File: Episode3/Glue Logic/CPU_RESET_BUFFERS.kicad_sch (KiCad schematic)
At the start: 28 parts, among them SW1 RST SW, U1 74AHCT541, U2 74HC245, U3 HD63C09P, U4 74AHCT541, U5 74AHCT244, U6 MIC1232

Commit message: Pushing back everything, due to PC reinstall.
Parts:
- removed RN6: 130Ω, Package_DIP:DIP-16_W7.62mm, symbol Device:R_Pack08
- removed U5: 74AHCT244, Package_DIP:DIP-20_W7.62mm_Socket, symbol 74xx:74HC244
- added R3, R4, R5: 100Ω, symbol Device:R_Small_US
- added U6: 74HCT125, symbol 74xx:74LS125
- U2: renamed from U6; symbol 6309 v2.0:MIC1232 -> MicroHobbyist:MIC1232
- U3: renamed from U1; value 74AHCT541 -> 74HCT541
- U4: value 74AHCT541 -> 74HCT541
- U5: renamed from U2; value 74HC245 -> 74HCT245
- renumbered R4 to R2, RN3 to RN1, RN4 to RN2, RN1 to RN3, RN5 to RN4, RN2 to RN5, U3 to U1
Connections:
- net UB_BS is gone; now on net BS: U1.5 (BS)
- net UB_Q is gone; now on net Q: U1.35 (Q)
- net +5V: now also U6.14 (VCC)
- net BA: now also R5.2; no longer U3.1 (G1), U4.1 (G1), U5.19 (CE)
- net E: now also R4.2
- net GND: now also U6.10, U6.12, U6.13, U6.4, U6.7 (GND)
- net R/~{W}: now also R3.2
- net UB_BA: now also U3.1 (G1), U4.1 (G1), U5.19 (CE), U6.1, U6.9
- net UB_E: now also U6.5
- net UB_R/~{W}: now also U6.2
- net ~{BREQ}: now also RN2.2 (R1); no longer RN2.4 (R3)
- net ~{HALT}: now also RN2.3 (R2); no longer RN2.2 (R1)
- net ~{MRDY}: now also RN2.4 (R3); no longer RN2.3 (R2)
- net ~{RST_{trigger}}: no longer names the net of SW1.2, U2.1 (~{PBRST})
- new net: R3.1, U6.3
- new net: R5.1, U6.8
- new net: R4.1, U6.6
- no-connect marks 4 -> 2
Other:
- moved on the sheet: JP1, R2, RN1, RN2, RN3, RN4, RN5, SW1, U1, U2

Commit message: Major updates to PLDs
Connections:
- net Q: now also U2.7 (~{ST})
- net UB_E: no longer U2.7 (~{ST})
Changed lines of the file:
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@@
+	)
+	(junction
+		(at 105.41 99.06)
+		(diameter 0)
+		(color 0 0 0 0)
 	)
 	(junction
@@
 	)
 	(junction
-		(at 105.41 96.52)
-		(diameter 0)
-		(color 0 0 0 0)
-	)
-	(junction
 		(at 44.45 68.58)
 		(diameter 0)
@@
 	(wire
 		(pts
-			(xy 105.41 96.52) (xy 179.07 96.52)
+			(xy 95.25 96.52) (xy 179.07 96.52)
 		)
 		(stroke
@@
 	(wire
 		(pts
+			(xy 105.41 99.06) (xy 240.03 99.06)
+		)
+		(stroke
+			(width 0)
+			(type default)
+		)
+	)
+	(wire
+		(pts
 			(xy 62.23 55.88) (xy 69.85 55.88)
 		)
@@
 		)
 	)
-	(wire
-		(pts
-			(xy 95.25 96.52) (xy 105.41 96.52)
-		)
-		(stroke
-			(width 0)
-			(type default)
-		)
-	)
 	(bus
 		(pts
@@
 	(wire
 		(pts
-			(xy 95.25 99.06) (xy 240.03 99.06)
+			(xy 95.25 99.06) (xy 105.41 99.06)
 		)
 		(stroke
@@
 	(wire
 		(pts
+			(xy 105.41 99.06) (xy 105.41 123.19)
+		)
+		(stroke
+			(width 0)
+			(type default)
+		)
+	)
+	(wire
+		(pts
 			(xy 224.79 45.72) (xy 232.41 45.72)
 		)
@@
 		)
 		(stroke
-			(width 0)
-			(type default)
-		)
-	)
-	(wire
-		(pts
-			(xy 105.41 96.52) (xy 105.41 123.19)
-		)
-		(stroke

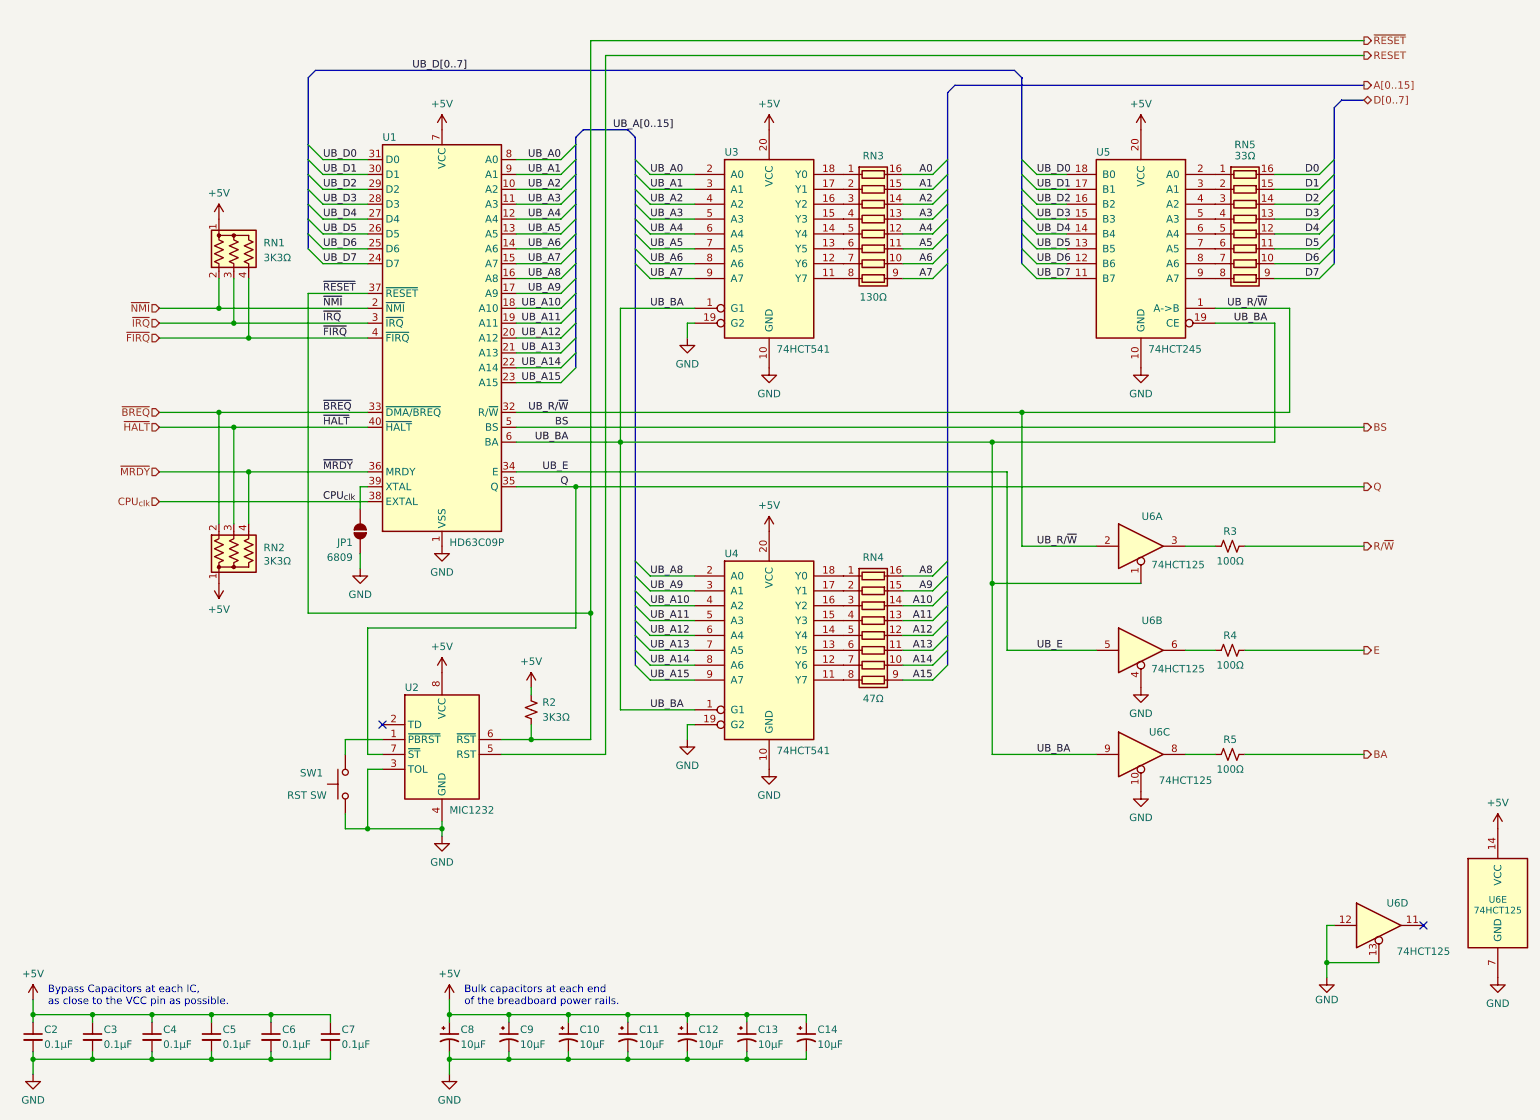
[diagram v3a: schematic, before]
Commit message: Reduced PLDs from 5 to 4, and optimized macrocells to the maximum
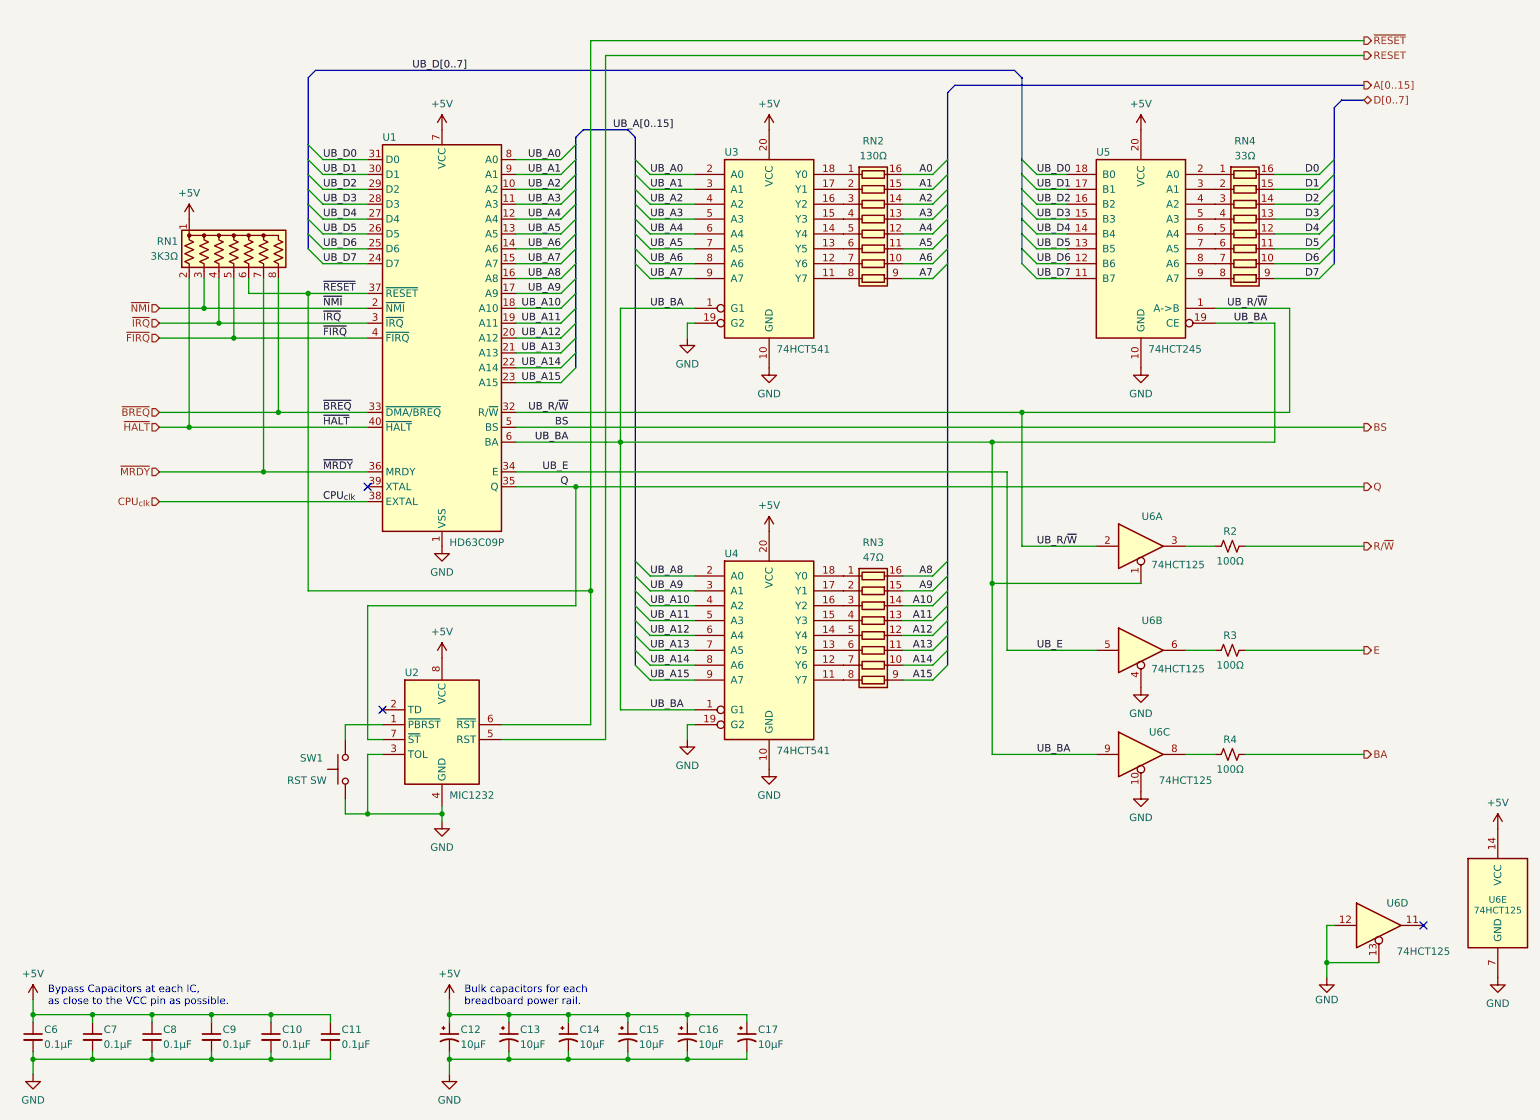
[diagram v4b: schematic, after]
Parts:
- removed C14: 10µF, symbol Device:C_Polarized_Small_US
- removed JP1: 6809, symbol Jumper:SolderJumper_2_Open
- removed R2: 3K3Ω, symbol Device:R_Small_US
- removed RN2: 3K3Ω, Resistor_THT:R_Array_SIP4, symbol Device:R_Network03_US
- RN1: footprint Resistor_THT:R_Array_SIP4 -> Resistor_THT:R_Array_SIP8; symbol Device:R_Network03_US -> Device:R_Network07_US
- renumbered C6 to C10, C7 to C11, C8 to C12, C9 to C13, C10 to C14, C11 to C15, C12 to C16, C13 to C17, C2 to C6, C3 to C7, C4 to C8, C5 to C9, R3 to R2, R4 to R3, R5 to R4, RN3 to RN2, RN4 to RN3, RN5 to RN4
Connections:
- net ~{BREQ}: now also RN1.8 (R7)
- net ~{FIRQ}: now also RN1.5 (R4); no longer RN1.4 (R3)
- net ~{HALT}: now also RN1.2 (R1)
- net ~{IRQ}: now also RN1.4 (R3); no longer RN1.3 (R2)
- net ~{MRDY}: now also RN1.7 (R6)
- net ~{NMI}: now also RN1.3 (R2); no longer RN1.2 (R1)
- net ~{RESET}: now also RN1.6 (R5)
- no-connect marks 2 -> 3
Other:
- note added: "Bulk capacitors for each breadboard power rail."
- note removed: "Bulk capacitors at each end of the breadboard power rails."
- moved on the sheet: SW1, U2

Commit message: Exploited every last macrocells I could.
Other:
- moved on the sheet: R2, R3, R4, RN1, RN2, RN3, RN4, SW1, U1, U2, U3, U4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
